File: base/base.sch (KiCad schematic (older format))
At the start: 19 parts, among them J1 FTDI, J2 CONN_01X04, J3 CONN_01X40, J4 CONN_01X08, SW1 SW_Push, U1 Z80CPU, U2 27C256, U3 7404, U4 55257, U5 7432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

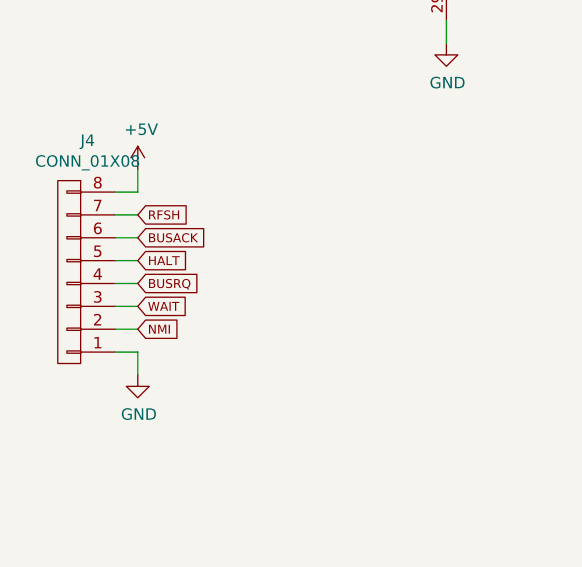
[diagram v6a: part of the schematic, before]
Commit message: Board layout for remaining pins
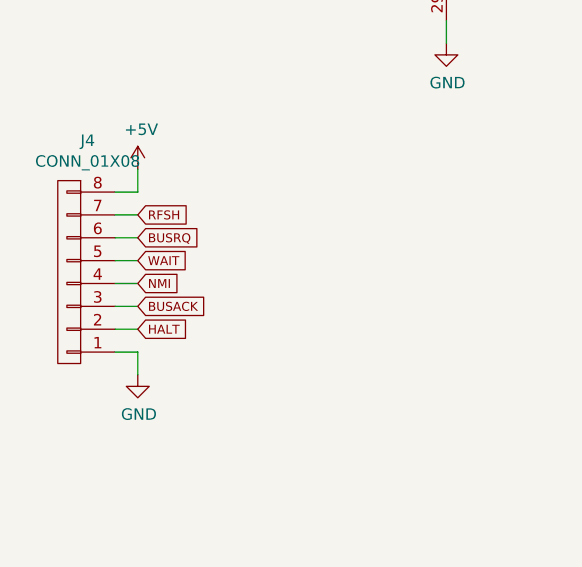
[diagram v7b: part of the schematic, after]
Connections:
- net BUSACK: now also J4.3 (P3); no longer J4.6 (P6)
- net BUSRQ: now also J4.6 (P6); no longer J4.4 (P4)
- net HALT: now also J4.2 (P2); no longer J4.5 (P5)
- net NMI: now also J4.4 (P4); no longer J4.2 (P2)
- net WAIT: now also J4.5 (P5); no longer J4.3 (P3)
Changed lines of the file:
@@
 Wire Wire Line
 	1150 6250 1050 6250
+Text GLabel 1150 6650 2    39   Input ~ 0
+BUSACK
+Text GLabel 1150 6750 2    39   Input ~ 0
+HALT
 Text GLabel 1150 6350 2    39   Input ~ 0
-BUSACK
+BUSRQ
 Text GLabel 1150 6450 2    39   Input ~ 0
-HALT
+WAIT
 Text GLabel 1150 6550 2    39   Input ~ 0
-BUSRQ
-Text GLabel 1150 6650 2    39   Input ~ 0
-WAIT
-Text GLabel 1150 6750 2    39   Input ~ 0
 NMI
 Wire Wire Line

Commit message: Clean up traces
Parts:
- removed JP1: CLK JMP, Pin_Headers:Pin_Header_Straight_1x02_Pitch2.54mm, symbol Jumper_NC_Small
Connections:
- net CLOCK: now also X1.5 (OUT)
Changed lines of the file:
@@
 A7
-$Comp
-L Jumper_NC_Small JP1
-U 1 1 596D4034
-P 1500 3000
-F 0 "JP1" H 1500 3212 50  0000 C CNN
-F 1 "CLK JMP" H 1500 3121 50  0000 C CNN
-F 2 "Pin_Headers:Pin_Header_Straight_1x02_Pitch2.54mm" H 1500 3000 50  0001 C CNN
-F 3 "" H 1500 3000 50  0001 C CNN
-	1    1500 3000
-	1    0    0    -1
-$EndComp
 $Comp
 L CONN_01X06 J1
@@
 	7550 1400 7550 1200
 Wire Wire Line
-	1250 3000 1400 3000
-Wire Wire Line
-	1600 3000 1800 3000
+	1250 3000 1800 3000
 Wire Wire Line
 	11650 3300 11750 3300
